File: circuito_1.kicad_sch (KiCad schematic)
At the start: 17 parts, among them J1 Conn_01x02, SW1 SW_SPDT, T1 Transformer_1P_2S, U4 LM7815_TO220, U5 LM7815_TO220

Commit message: Reorganização dos esquemáticos em pages.
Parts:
- removed C1, C2: 2200uF/35v, symbol Device:C_Polarized
- removed C3, C4, C5, C6: 100nF/50v, symbol Device:C
- removed D1, D2, D3, D4: 1N4007, Diode_THT:D_DO-41_SOD81_P10.16mm_Horizontal, symbol Diode:1N4007
- removed F1: Fuse, symbol Device:Fuse
- removed J1: Conn_01x02, symbol Connector_Generic:Conn_01x02
- removed RV1: Varistor, symbol Device:Varistor
- removed SW1: SW_SPDT, symbol Switch:SW_SPDT
- removed T1: Transformer_1P_2S, symbol Device:Transformer_1P_2S
- removed U4, U5: LM7815_TO220, Package_TO_SOT_THT:TO-220-3_Vertical, symbol Regulator_Linear:LM7815_TO220
- added C16, C17: 2200uF/35v, symbol Device:C_Polarized
- added C18, C19, C20, C21: 100nF/50v, symbol Device:C
- added D5, D6, D7, D8: 1N4007, Diode_THT:D_DO-41_SOD81_P10.16mm_Horizontal, symbol Diode:1N4007
- added F2: Fuse, symbol Device:Fuse
- added J2: Conn_01x02, symbol Connector_Generic:Conn_01x02
- added RV2: Varistor, symbol Device:Varistor
- added SW2: SW_SPDT, symbol Switch:SW_SPDT
- added T2: Transformer_1P_2S, symbol Device:Transformer_1P_2S
- added U6, U7: LM7815_TO220, Package_TO_SOT_THT:TO-220-3_Vertical, symbol Regulator_Linear:LM7815_TO220
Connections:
- net +15V: now also C20.1, U6.3 (VO)
- net -15V: now also C17.2, C19.2, C21.2, D6.2 (A), D8.2 (A), U7.1 (VI), U7.3 (VO)
- net GND: now also C16.2, C17.1, C18.2, C19.1, C20.2, C21.1, T2.4 (SB), T2.5 (SC), U6.2 (GND), U7.2 (GND)
- new net: C16.1, C18.1, D5.1 (K), D7.1 (K), U6.1 (VI)
- new net: D7.2 (A), D8.1 (K), T2.6 (SD)
- new net: J2.1 (Pin_1), RV2.2, T2.2 (AB)
- new net: F2.2, J2.2 (Pin_2)
- new net: F2.1, RV2.1, SW2.2 (B)
- new net: SW2.3 (C), T2.1 (AA)
- new net: D5.2 (A), D6.1 (K), T2.3 (SA)

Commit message: Footprints parcialmente adicionados.
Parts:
- C1: renamed from C16; footprint (none) -> Capacitor_THT:CP_Radial_D10.0mm_P3.50mm
- C2: renamed from C17; footprint (none) -> Capacitor_THT:CP_Radial_D10.0mm_P3.50mm
- C3: renamed from C18; footprint (none) -> Capacitor_THT:C_Disc_D3.8mm_W2.6mm_P2.50mm
- C4: renamed from C19; footprint (none) -> Capacitor_THT:C_Disc_D3.8mm_W2.6mm_P2.50mm
- C5: renamed from C20; footprint (none) -> Capacitor_THT:C_Disc_D3.8mm_W2.6mm_P2.50mm
- C6: renamed from C21; footprint (none) -> Capacitor_THT:C_Disc_D3.8mm_W2.6mm_P2.50mm
- D1: renamed from D5; footprint Diode_THT:D_DO-41_SOD81_P10.16mm_Horizontal -> (none)
- D2: renamed from D6; footprint Diode_THT:D_DO-41_SOD81_P10.16mm_Horizontal -> (none)
- D3: renamed from D7; footprint Diode_THT:D_DO-41_SOD81_P10.16mm_Horizontal -> (none)
- D4: renamed from D8; footprint Diode_THT:D_DO-41_SOD81_P10.16mm_Horizontal -> (none)
- U1: renamed from U6; footprint Package_TO_SOT_THT:TO-220-3_Vertical -> (none)
- U2: renamed from U7; footprint Package_TO_SOT_THT:TO-220-3_Vertical -> (none)
- renumbered F2 to F1, J2 to J1, RV2 to RV1, SW2 to SW1, T2 to T1
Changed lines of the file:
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@@
 		(dnp no)
 		(fields_autoplaced yes)
-		(property "Reference" "#PWR025"
+		(property "Reference" "#PWR04"
 			(at 204.47 109.22 0)
 			(effects
@@
 			(project "contr-disp-digitais"
 				(path "/99929c84-d1b2-45a3-8153-a7b417c53f39/cc7337dc-c2d7-4fcb-b466-4da1a29a0de2"
-					(reference "#PWR025")
+					(reference "#PWR04")
 					(unit 1)
 				)
@@
 		(dnp no)
 		(fields_autoplaced yes)
-		(property "Reference" "#PWR023"
+		(property "Reference" "#PWR02"
 			(at 167.64 73.66 0)
 			(effects
@@
 			(project "contr-disp-digitais"
 				(path "/99929c84-d1b2-45a3-8153-a7b417c53f39/cc7337dc-c2d7-4fcb-b466-4da1a29a0de2"
-					(reference "#PWR023")
+					(reference "#PWR02")
 					(unit 1)
 				)
@@
 		(dnp no)
 		(fields_autoplaced yes)
-		(property "Reference" "C17"
+		(property "Reference" "C2"
 			(at 163.83 90.5509 0)
 			(effects
@@
 			)
 		)
-		(property "Footprint" ""
+		(property "Footprint" "Capacitor_THT:CP_Radial_D10.0mm_P3.50mm"
 			(at 160.9852 96.52 0)
 			(effects
@@
 			(project "contr-disp-digitais"
 				(path "/99929c84-d1b2-45a3-8153-a7b417c53f39/cc7337dc-c2d7-4fcb-b466-4da1a29a0de2"
-					(reference "C17")
+					(reference "C2")
 					(unit 1)
 				)
@@
 		(dnp no)
 		(fields_autoplaced yes)
-		(property "Reference" "C16"
+		(property "Reference" "C1"
 			(at 163.83 52.4509 0)
 			(effects
@@
 			)
 		)
-		(property "Footprint" ""
+		(property "Footprint" "Capacitor_THT:CP_Radial_D10.0mm_P3.50mm"
 			(at 160.9852 58.42 0)
 			(effects
@@
 			(project "contr-disp-digitais"
 				(path "/99929c84-d1b2-45a3-8153-a7b417c53f39/cc7337dc-c2d7-4fcb-b466-4da1a29a0de2"
-					(reference "C16")
+					(reference "C1")
 					(unit 1)
 				)
@@
 		(dnp no)
 		(fields_autoplaced yes)
-		(property "Reference" "U6"
+		(property "Reference" "U1"
 			(at 203.2 39.37 0)
 			(effects
@@
 			)
 		)
-		(property "Footprint" "Package_TO_SOT_THT:TO-220-3_Vertical"
+		(property "Footprint" ""
 			(at 203.2 40.005 0)
 			(effects
@@
 			(project "contr-disp-digitais"
 				(path "/99929c84-d1b2-45a3-8153-a7b417c53f39/cc7337dc-c2d7-4fcb-b466-4da1a29a0de2"
-					(reference "U6")
+					(reference "U1")
 					(unit 1)
 				)
@@
 		(on_board yes)
 		(dnp no)
-		(property "Reference" "U7"
+		(property "Reference" "U2"
 			(at 203.2 104.14 0)
 			(effects
@@
 			)
 		)
-		(property "Footprint" "Package_TO_SOT_THT:TO-220-3_Vertical"
+		(property "Footprint" ""
 			(at 203.2 106.045 0)
 			(effects
@@
 			(project "contr-disp-digitais"
 				(path "/99929c84-d1b2-45a3-8153-a7b417c53f39/cc7337dc-c2d7-4fcb-b466-4da1a29a0de2"
-					(reference "U7")
+					(reference "U2")
 					(unit 1)
 				)
@@
 		(dnp no)
 		(fields_autoplaced yes)
-		(property "Reference" "D8"
+		(property "Reference" "D4"
 			(at 146.05 90.1699 90)
 			(effects
@@
 			)
 		)
-		(property "Footprint" "Diode_THT:D_DO-41_SOD81_P10.16mm_Horizontal"
+		(property "Footprint" ""
 			(at 139.065 91.44 0)
 			(effects
@@
 			(project "contr-disp-digitais"
 				(path "/99929c84-d1b2-45a3-8153-a7b417c53f39/cc7337dc-c2d7-4fcb-b466-4da1a29a0de2"
-					(reference "D8")
+					(reference "D4")
 					(unit 1)
 				)
@@
 		(dnp no)
 		(fields_autoplaced yes)
-		(property "Reference" "J2"
+		(property "Reference" "J1"
 			(at 39.37 72.39 0)
 			(effects
@@
 			(project "contr-disp-digitais"
 				(path "/99929c84-d1b2-45a3-8153-a7b417c53f39/cc7337dc-c2d7-4fcb-b466-4da1a29a0de2"
-					(reference "J2")
+					(reference "J1")
 					(unit 1)
 				)
@@
 		(dnp no)
 		(fields_autoplaced yes)
-		(property "Reference" "SW2"
+		(property "Reference" "SW1"
 			(at 73.66 44.45 0)
 			(effects
@@
 			(project "contr-disp-digitais"
 				(path "/99929c84-d1b2-45a3-8153-a7b417c53f39/cc7337dc-c2d7-4fcb-b466-4da1a29a0de2"
-					(reference "SW2")
+					(reference "SW1")
 					(unit 1)
 				)
@@
 		(dnp no)
 		(fields_autoplaced yes)
-		(property "Reference" "F2"
+		(property "Reference" "F1"
 			(at 48.26 60.9599 0)
 			(effects
@@
 			(project "contr-disp-digitais"
 				(path "/99929c84-d1b2-45a3-8153-a7b417c53f39/cc7337dc-c2d7-4fcb-b466-4da1a29a0de2"
-					(reference "F2")
+					(reference "F1")
 					(unit 1)
 				)
@@
 		(dnp no)
 		(fields_autoplaced yes)
-		(property "Reference" "T2"
+		(property "Reference" "T1"
 			(at 100.33 57.15 0)
 			(effects
@@
 			(project "contr-disp-digitais"
 				(path "/99929c84-d1b2-45a3-8153-a7b417c53f39/cc7337dc-c2d7-4fcb-b466-4da1a29a0de2"
-					(reference "T2")
+					(reference "T1")
 					(unit 1)
 				)
@@
 		(dnp no)
 		(fields_autoplaced yes)
-		(property "Reference" "C19"
+		(property "Reference" "C4"
 			(at 184.15 91.4399 0)
 			(effects
@@
 			)
 		)
-		(property "Footprint" ""
+		(property "Footprint" "Capacitor_THT:C_Disc_D3.8mm_W2.6mm_P2.50mm"
 			(at 181.3052 96.52 0)
 			(effects
@@
 			(project "contr-disp-digitais"
 				(path "/99929c84-d1b2-45a3-8153-a7b417c53f39/cc7337dc-c2d7-4fcb-b466-4da1a29a0de2"
-					(reference "C19")
+					(reference "C4")
 					(unit 1)
 				)
@@
 		(dnp no)
 		(fields_autoplaced yes)
-		(property "Reference" "RV2"
+		(property "Reference" "RV1"
 			(at 64.77 71.3132 0)
 			(effects
@@
 			(project "contr-disp-digitais"
 				(path "/99929c84-d1b2-45a3-8153-a7b417c53f39/cc7337dc-c2d7-4fcb-b466-4da1a29a0de2"
-					(reference "RV2")
+					(reference "RV1")
 					(unit 1)
 				)
@@
 		(dnp no)
 		(fields_autoplaced yes)
-		(property "Reference" "C20"
+		(property "Reference" "C5"
 			(at 228.6 53.3399 0)
 			(effects
@@
 			)
 		)
-		(property "Footprint" ""
+		(property "Footprint" "Capacitor_THT:C_Disc_D3.8mm_W2.6mm_P2.50mm"
 			(at 225.7552 58.42 0)
 			(effects
@@
 			(project "contr-disp-digitais"
 				(path "/99929c84-d1b2-45a3-8153-a7b417c53f39/cc7337dc-c2d7-4fcb-b466-4da1a29a0de2"
-					(reference "C20")
+					(reference "C5")
 					(unit 1)
 				)
@@
 		(dnp no)
 		(fields_autoplaced yes)
-		(property "Reference" "#PWR024"
+		(property "Reference" "#PWR03"
 			(at 187.96 73.66 0)
 			(effects
@@
 			(project "contr-disp-digitais"
 				(path "/99929c84-d1b2-45a3-8153-a7b417c53f39/cc7337dc-c2d7-4fcb-b466-4da1a29a0de2"
-					(reference "#PWR024")
+					(reference "#PWR03")
 					(unit 1)
 				)
@@
 		(dnp no)
 		(fields_autoplaced yes)
-		(property "Reference" "C18"
+		(property "Reference" "C3"
 			(at 184.15 53.3399 0)
 			(effects
@@
 			)
 		)
-		(property "Footprint" ""
+		(property "Footprint" "Capacitor_THT:C_Disc_D3.8mm_W2.6mm_P2.50mm"
 			(at 181.3052 58.42 0)
 			(effects
@@
 			(project "contr-disp-digitais"
 				(path "/99929c84-d1b2-45a3-8153-a7b417c53f39/cc7337dc-c2d7-4fcb-b466-4da1a29a0de2"
-					(reference "C18")
+					(reference "C3")
 					(unit 1)
 				)
@@
 		(dnp no)
 		(fields_autoplaced yes)
-		(property "Reference" "D6"
+		(property "Reference" "D2"
 			(at 123.19 90.1699 90)
 			(effects
@@
 			)
 		)
-		(property "Footprint" "Diode_THT:D_DO-41_SOD81_P10.16mm_Horizontal"
+		(property "Footprint" ""
 			(at 116.205 91.44 0)
 			(effects
@@
 			(project "contr-disp-digitais"
 				(path "/99929c84-d1b2-45a3-8153-a7b417c53f39/cc7337dc-c2d7-4fcb-b466-4da1a29a0de2"
-					(reference "D6")
+					(reference "D2")
 					(unit 1)
 				)
@@
 		(dnp no)
 		(fields_autoplaced yes)
-		(property "Reference" "C21"
+		(property "Reference" "C6"
 			(at 228.6 92.7099 0)
 			(effects
@@
 			)
 		)
-		(property "Footprint" ""
+		(property "Footprint" "Capacitor_THT:C_Disc_D3.8mm_W2.6mm_P2.50mm"
 			(at 225.7552 97.79 0)
 			(effects
@@
 			(project "contr-disp-digitais"
 				(path "/99929c84-d1b2-45a3-8153-a7b417c53f39/cc7337dc-c2d7-4fcb-b466-4da1a29a0de2"
-					(reference "C21")
+					(reference "C6")
 					(unit 1)
 				)
@@
 		(on_board yes)
 		(dnp no)
-		(property "Reference" "#PWR028"
+		(property "Reference" "#PWR07"
 			(at 233.68 73.66 0)
 			(effects
@@
 			(project "contr-disp-digitais"
 				(path "/99929c84-d1b2-45a3-8153-a7b417c53f39/cc7337dc-c2d7-4fcb-b466-4da1a29a0de2"
-					(reference "#PWR028")
+					(reference "#PWR07")
 					(unit 1)
 				)
@@
 		(dnp no)
 		(fields_autoplaced yes)
-		(property "Reference" "D5"
+		(property "Reference" "D1"
 			(at 123.19 53.3399 90)
 			(effects
@@
 			)
 		)
-		(property "Footprint" "Diode_THT:D_DO-41_SOD81_P10.16mm_Horizontal"
+		(property "Footprint" ""
 			(at 116.205 54.61 0)
 			(effects
@@
 			(project "contr-disp-digitais"
 				(path "/99929c84-d1b2-45a3-8153-a7b417c53f39/cc7337dc-c2d7-4fcb-b466-4da1a29a0de2"
-					(reference "D5")
+					(reference "D1")
 					(unit 1)
 				)
@@
 		(dnp no)
 		(fields_autoplaced yes)
-		(property "Reference" "#PWR027"
+		(property "Reference" "#PWR06"
 			(at 224.79 40.64 0)
 			(effects
@@
 			(project "contr-disp-digitais"
 				(path "/99929c84-d1b2-45a3-8153-a7b417c53f39/cc7337dc-c2d7-4fcb-b466-4da1a29a0de2"
-					(reference "#PWR027")
+					(reference "#PWR06")
 					(unit 1)
 				)
@@
 		(dnp no)
 		(fields_autoplaced yes)
-		(property "Reference" "D7"
+		(property "Reference" "D3"
 			(at 146.05 53.3399 90)
 			(effects
@@
 			)
 		)
-		(property "Footprint" "Diode_THT:D_DO-41_SOD81_P10.16mm_Horizontal"
+		(property "Footprint" ""
 			(at 139.065 54.61 0)
 			(effects
@@
 			(project "contr-disp-digitais"
 				(path "/99929c84-d1b2-45a3-8153-a7b417c53f39/cc7337dc-c2d7-4fcb-b466-4da1a29a0de2"
-					(reference "D7")
+					(reference "D3")
 					(unit 1)
 				)
@@
 		(dnp no)
 		(fields_autoplaced yes)
-		(property "Reference" "#PWR022"
+		(property "Reference" "#PWR01"
 			(at 119.38 72.39 0)
 			(effects
@@
 			(project "contr-disp-digitais"
 				(path "/99929c84-d1b2-45a3-8153-a7b417c53f39/cc7337dc-c2d7-4fcb-b466-4da1a29a0de2"
-					(reference "#PWR022")
+					(reference "#PWR01")
 					(unit 1)
 				)
@@
 		(dnp no)
 		(fields_autoplaced yes)
-		(property "Reference" "#PWR026"
+		(property "Reference" "#PWR05"
 			(at 212.09 73.66 0)
 			(effects
@@
 			(project "contr-disp-digitais"
 				(path "/99929c84-d1b2-45a3-8153-a7b417c53f39/cc7337dc-c2d7-4fcb-b466-4da1a29a0de2"
-					(reference "#PWR026")
-					(unit 1)
-				)
+					(reference "#PWR05")
+					(unit 1)
+				)

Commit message: Relação de footprints finalizada.
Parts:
- D1, D2, D3, D4: footprint (none) -> Diode_THT:D_DO-41_SOD81_P10.16mm_Horizontal
- F1: footprint (none) -> Fuse:Fuseholder_Clip-5x20mm_Keystone_3512P_Inline_P23.62x7.27mm_D1.02x2.41x1.02x1.57mm_Horizontal
- J1: footprint (none) -> TerminalBlock_Phoenix:TerminalBlock_Phoenix_MKDS-1,5-2-5.08_1x02_P5.08mm_Horizontal
- RV1: footprint (none) -> Varistor:RV_Disc_D12mm_W4.7mm_P7.5mm
- SW1: footprint (none) -> Button_Switch_THT:SW_NKK_BB15AH
- T1: footprint (none) -> Transformer_THT:Transformer_CHK_EI48-8VA_2xSec
- U1, U2: footprint (none) -> Package_TO_SOT_THT:TO-220-3_Vertical
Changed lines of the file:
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@@
 			)
 		)
-		(property "Footprint" ""
+		(property "Footprint" "Package_TO_SOT_THT:TO-220-3_Vertical"
 			(at 203.2 40.005 0)
 			(effects
@@
 			)
 		)
-		(property "Footprint" ""
+		(property "Footprint" "Package_TO_SOT_THT:TO-220-3_Vertical"
 			(at 203.2 106.045 0)
 			(effects
@@
 			)
 		)
-		(property "Footprint" ""
+		(property "Footprint" "Diode_THT:D_DO-41_SOD81_P10.16mm_Horizontal"
 			(at 139.065 91.44 0)
 			(effects
@@
 			)
 		)
-		(property "Footprint" ""
+		(property "Footprint" "TerminalBlock_Phoenix:TerminalBlock_Phoenix_MKDS-1,5-2-5.08_1x02_P5.08mm_Horizontal"
 			(at 39.37 81.28 0)
 			(effects
@@
 			)
 		)
-		(property "Footprint" ""
+		(property "Footprint" "Button_Switch_THT:SW_NKK_BB15AH"
 			(at 73.66 53.34 0)
 			(effects
@@
 			)
 		)
-		(property "Footprint" ""
+		(property "Footprint" "Fuse:Fuseholder_Clip-5x20mm_Keystone_3512P_Inline_P23.62x7.27mm_D1.02x2.41x1.02x1.57mm_Horizontal"
 			(at 43.942 62.23 90)
 			(effects
@@
 			)
 		)
-		(property "Footprint" ""
+		(property "Footprint" "Transformer_THT:Transformer_CHK_EI48-8VA_2xSec"
 			(at 100.33 72.39 0)
 			(effects
@@
 			)
 		)
-		(property "Footprint" ""
+		(property "Footprint" "Varistor:RV_Disc_D12mm_W4.7mm_P7.5mm"
 			(at 60.452 72.39 90)
 			(effects
@@
 			)
 		)
-		(property "Footprint" ""
+		(property "Footprint" "Diode_THT:D_DO-41_SOD81_P10.16mm_Horizontal"
 			(at 116.205 91.44 0)
 			(effects
@@
 			)
 		)
-		(property "Footprint" ""
+		(property "Footprint" "Diode_THT:D_DO-41_SOD81_P10.16mm_Horizontal"
 			(at 116.205 54.61 0)
 			(effects
@@
 			)
 		)
-		(property "Footprint" ""
+		(property "Footprint" "Diode_THT:D_DO-41_SOD81_P10.16mm_Horizontal"
 			(at 139.065 54.61 0)
 			(effects

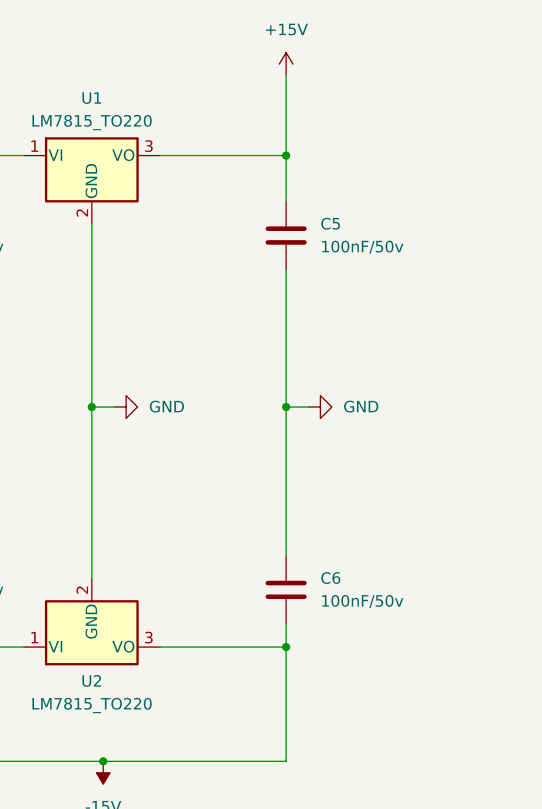
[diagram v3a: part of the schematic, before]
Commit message: Alterações no schematic para bater com o que o professor mandoou no gropo. Pendente revisão.
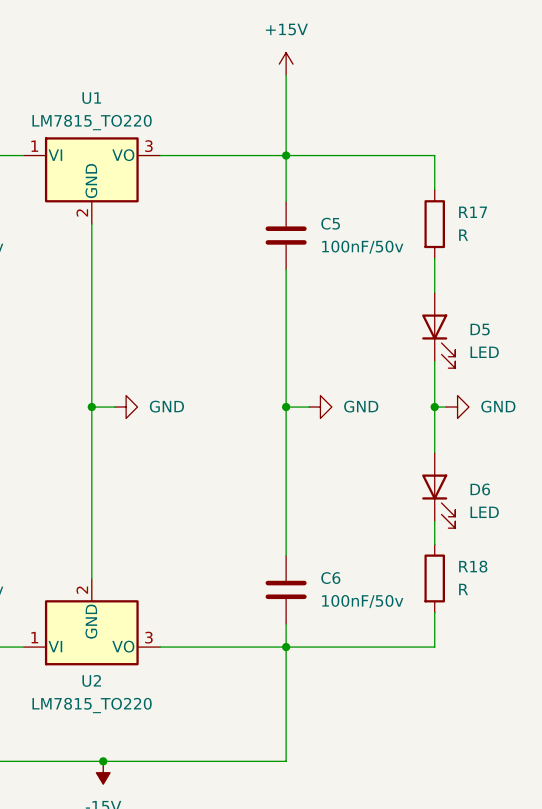
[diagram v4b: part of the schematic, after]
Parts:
- added D5, D6: LED, LED_SMD:LED_0805_2012Metric, symbol Device:LED
- added R17, R18: R, Resistor_SMD:R_0805_2012Metric, symbol Device:R
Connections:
- net +15V: now also R17.1
- net -15V: now also R18.2
- net GND: now also D5.1 (K), D6.2 (A)
- new net: D5.2 (A), R17.2
- new net: D6.1 (K), R18.1

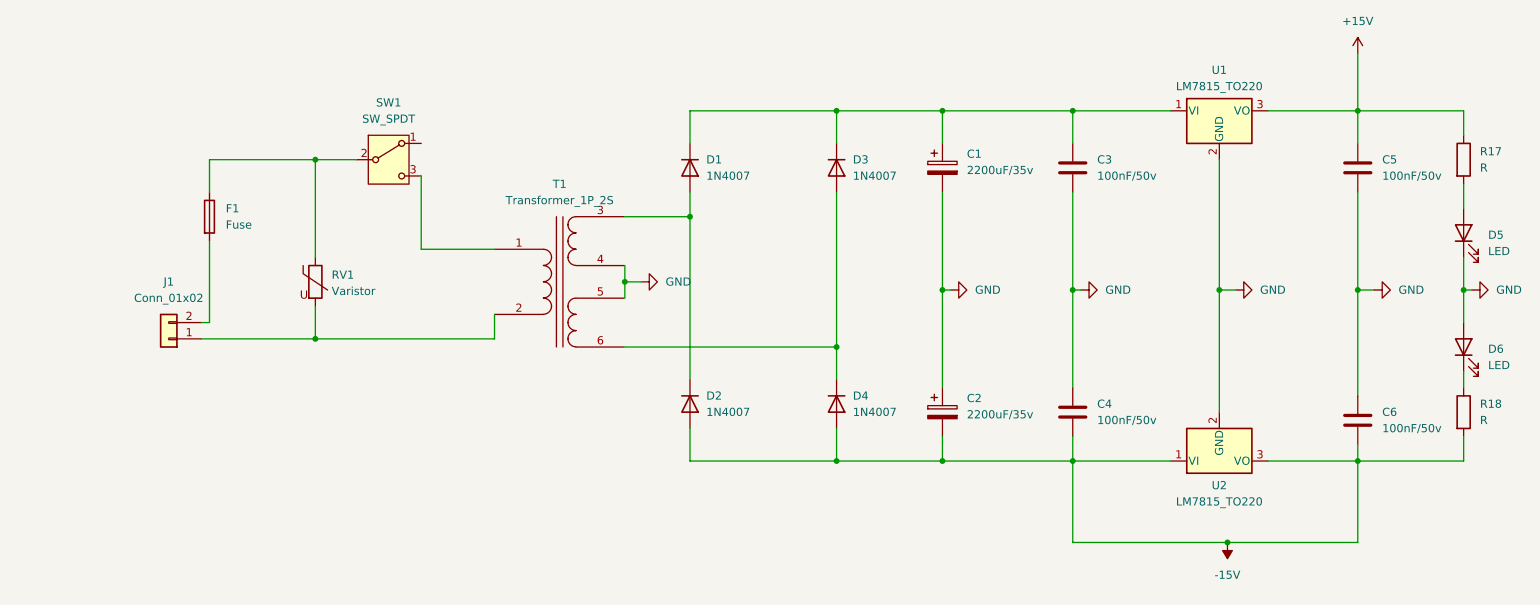
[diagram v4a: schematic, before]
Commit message: Revisão de schematics finalizado. Posicionamentos dos componentes do circuito 1 e 2 no PCB editor.
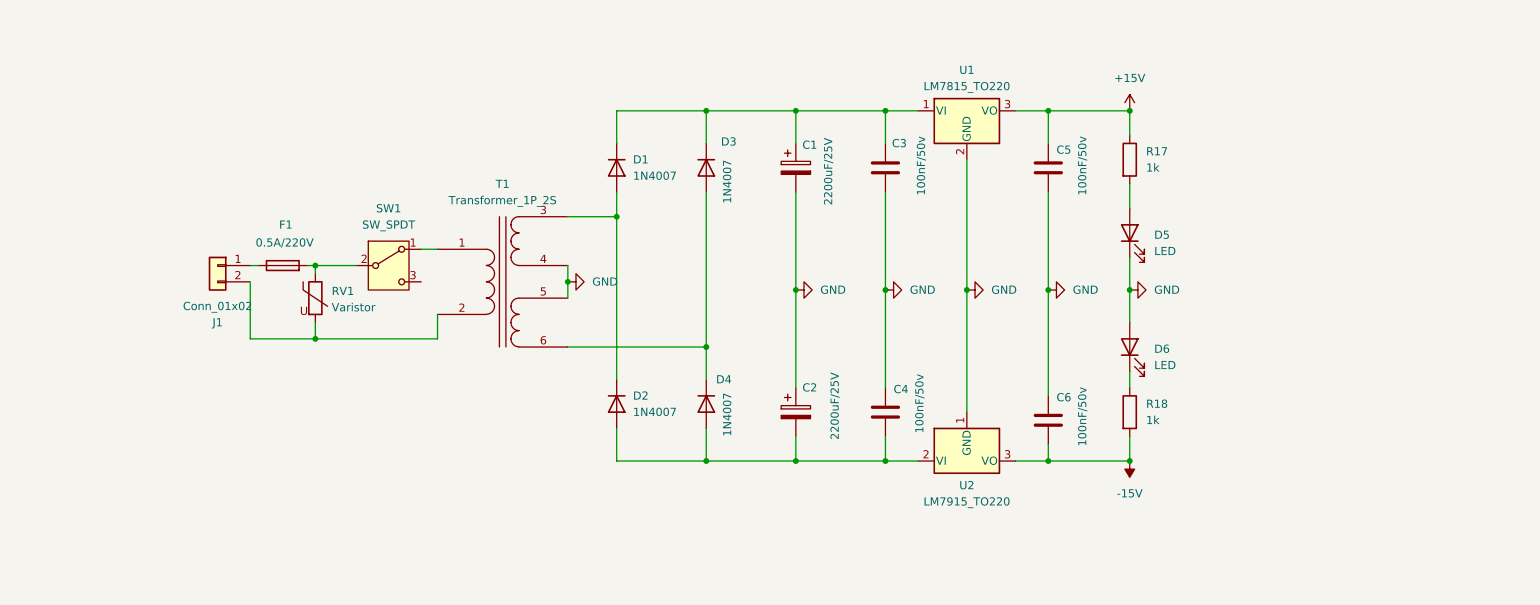
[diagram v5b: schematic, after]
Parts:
- removed U2: LM7815_TO220, Package_TO_SOT_THT:TO-220-3_Vertical, symbol Regulator_Linear:LM7815_TO220
- added U2: LM7915_TO220, Package_TO_SOT_THT:TO-220-3_Vertical, symbol Regulator_Linear:LM7915_TO220
- C1, C2: value 2200uF/35v -> 2200uF/25V
- C3, C4, C5, C6: footprint Capacitor_THT:C_Disc_D3.8mm_W2.6mm_P2.50mm -> Capacitor_THT:C_Disc_D3.4mm_W2.1mm_P2.50mm
- F1: value Fuse -> 0.5A/220V
- R17, R18: value R -> 1k
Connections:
- net -15V: now also U2.3 (VO); no longer C2.2, C4.2, D2.2 (A), D4.2 (A)
- net GND: now also U2.1 (GND)
- net at RV1.2, T1.2 (AB): now also J1.2 (Pin_2); no longer J1.1 (Pin_1)
- net at F1.2: now also RV1.1, SW1.2 (B); no longer J1.2 (Pin_2)
- net at SW1.1 (A): now also T1.1 (AA)
- net at SW1.3 (C): no longer T1.1 (AA)
- new net: C2.2, C4.2, D2.2 (A), D4.2 (A), U2.2 (VI)
- new net: F1.1, J1.1 (Pin_1)
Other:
- moved on the sheet: C1, C2, C3, C4, C5, C6, D1, D2, D3, D4, D5, D6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
